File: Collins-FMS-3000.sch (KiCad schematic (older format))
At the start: 24 parts, among them J3 Conn_02x04_Odd_Even, U2 MCP23017_SO, U3 MCP23017_SO, U4 IS31FL3733B

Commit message: Use perfect 0402 pad dimensions
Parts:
- C1, C2, C22, C23, C24, C25, C26, C27, C28, C3, C4: footprint Capacitor_SMD:C_0402_1005Metric -> Collins-FMS-3000:Perfect_0402
- R6, R7: footprint Resistor_SMD:R_0402_1005Metric -> Collins-FMS-3000:Perfect_0402
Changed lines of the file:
@@
 F 0 "C2" H 3442 3196 50  0000 L CNN
 F 1 "100nf" H 3442 3105 50  0000 L CNN
-F 2 "Capacitor_SMD:C_0402_1005Metric" H 3350 3150 50  0001 C CNN
+F 2 "Collins-FMS-3000:Perfect_0402" H 3350 3150 50  0001 C CNN
 F 3 "~" H 3350 3150 50  0001 C CNN
 F 4 "0402" H 3350 3150 50  0001 C CNN "JLC"
@@
 F 0 "C1" H 3092 3196 50  0000 L CNN
 F 1 "1uF" H 3092 3105 50  0000 L CNN
-F 2 "Capacitor_SMD:C_0402_1005Metric" H 3000 3150 50  0001 C CNN
+F 2 "Collins-FMS-3000:Perfect_0402" H 3000 3150 50  0001 C CNN
 F 3 "~" H 3000 3150 50  0001 C CNN
 F 4 "0402" H 3000 3150 50  0001 C CNN "JLC"
@@
 F 0 "C4" H 4192 3196 50  0000 L CNN
 F 1 "100nf" H 4192 3105 50  0000 L CNN
-F 2 "Capacitor_SMD:C_0402_1005Metric" H 4100 3150 50  0001 C CNN
+F 2 "Collins-FMS-3000:Perfect_0402" H 4100 3150 50  0001 C CNN
 F 3 "~" H 4100 3150 50  0001 C CNN
 F 4 "0402" H 4100 3150 50  0001 C CNN "JLC"
@@
 F 0 "C3" H 3842 3196 50  0000 L CNN
 F 1 "1uF" H 3842 3105 50  0000 L CNN
-F 2 "Capacitor_SMD:C_0402_1005Metric" H 3750 3150 50  0001 C CNN
+F 2 "Collins-FMS-3000:Perfect_0402" H 3750 3150 50  0001 C CNN
 F 3 "~" H 3750 3150 50  0001 C CNN
 F 4 "0402" H 3750 3150 50  0001 C CNN "JLC"
@@
 F 0 "C22" H 6892 1246 50  0000 L CNN
 F 1 "470nf" H 6892 1155 50  0000 L CNN
-F 2 "Capacitor_SMD:C_0402_1005Metric" H 6800 1200 50  0001 C CNN
+F 2 "Collins-FMS-3000:Perfect_0402" H 6800 1200 50  0001 C CNN
 F 3 "~" H 6800 1200 50  0001 C CNN
 F 4 "0402" H 6800 1200 50  0001 C CNN "JLC"
@@
 F 0 "C25" H 7292 1246 50  0000 L CNN
 F 1 "100nf" H 7292 1155 50  0000 L CNN
-F 2 "Capacitor_SMD:C_0402_1005Metric" H 7200 1200 50  0001 C CNN
+F 2 "Collins-FMS-3000:Perfect_0402" H 7200 1200 50  0001 C CNN
 F 3 "~" H 7200 1200 50  0001 C CNN
 F 4 "0402" H 7200 1200 50  0001 C CNN "JLC"
@@
 F 0 "C23" H 6892 1546 50  0000 L CNN
 F 1 "470nf" H 6892 1455 50  0000 L CNN
-F 2 "Capacitor_SMD:C_0402_1005Metric" H 6800 1500 50  0001 C CNN
+F 2 "Collins-FMS-3000:Perfect_0402" H 6800 1500 50  0001 C CNN
 F 3 "~" H 6800 1500 50  0001 C CNN
 F 4 "0402" H 6800 1500 50  0001 C CNN "JLC"
@@
 F 0 "C26" H 7292 1546 50  0000 L CNN
 F 1 "100nf" H 7292 1455 50  0000 L CNN
-F 2 "Capacitor_SMD:C_0402_1005Metric" H 7200 1500 50  0001 C CNN
+F 2 "Collins-FMS-3000:Perfect_0402" H 7200 1500 50  0001 C CNN
 F 3 "~" H 7200 1500 50  0001 C CNN
 F 4 "0402" H 7200 1500 50  0001 C CNN "JLC"
@@
 F 0 "C24" H 6892 1896 50  0000 L CNN
 F 1 "470nf" H 6892 1805 50  0000 L CNN
-F 2 "Capacitor_SMD:C_0402_1005Metric" H 6800 1850 50  0001 C CNN
+F 2 "Collins-FMS-3000:Perfect_0402" H 6800 1850 50  0001 C CNN
 F 3 "~" H 6800 1850 50  0001 C CNN
 F 4 "0402" H 6800 1850 50  0001 C CNN "JLC"
@@
 F 0 "C27" H 7292 1896 50  0000 L CNN
 F 1 "100nf" H 7292 1805 50  0000 L CNN
-F 2 "Capacitor_SMD:C_0402_1005Metric" H 7200 1850 50  0001 C CNN
+F 2 "Collins-FMS-3000:Perfect_0402" H 7200 1850 50  0001 C CNN
 F 3 "~" H 7200 1850 50  0001 C CNN
 F 4 "0402" H 7200 1850 50  0001 C CNN "JLC"
@@
 F 0 "C28" H 7292 3196 50  0000 L CNN
 F 1 "470nf" H 7292 3105 50  0000 L CNN
-F 2 "Capacitor_SMD:C_0402_1005Metric" H 7200 3150 50  0001 C CNN
+F 2 "Collins-FMS-3000:Perfect_0402" H 7200 3150 50  0001 C CNN
 F 3 "~" H 7200 3150 50  0001 C CNN
 F 4 "0402" H 7200 3150 50  0001 C CNN "JLC"
@@
 F 0 "R7" H 6909 2896 50  0000 L CNN
 F 1 "100k" H 6909 2805 50  0000 L CNN
-F 2 "Resistor_SMD:R_0402_1005Metric" H 6850 2850 50  0001 C CNN
+F 2 "Collins-FMS-3000:Perfect_0402" H 6850 2850 50  0001 C CNN
 F 3 "~" H 6850 2850 50  0001 C CNN
 F 4 "0402" H 6850 2850 50  0001 C CNN "JLC"
@@
 F 0 "R6" H 6759 3746 50  0000 L CNN
 F 1 "47k" H 6759 3655 50  0000 L CNN
-F 2 "Resistor_SMD:R_0402_1005Metric" H 6700 3700 50  0001 C CNN
+F 2 "Collins-FMS-3000:Perfect_0402" H 6700 3700 50  0001 C CNN
 F 3 "~" H 6700 3700 50  0001 C CNN
 F 4 "0402" H 6700 3700 50  0001 C CNN "JLC"

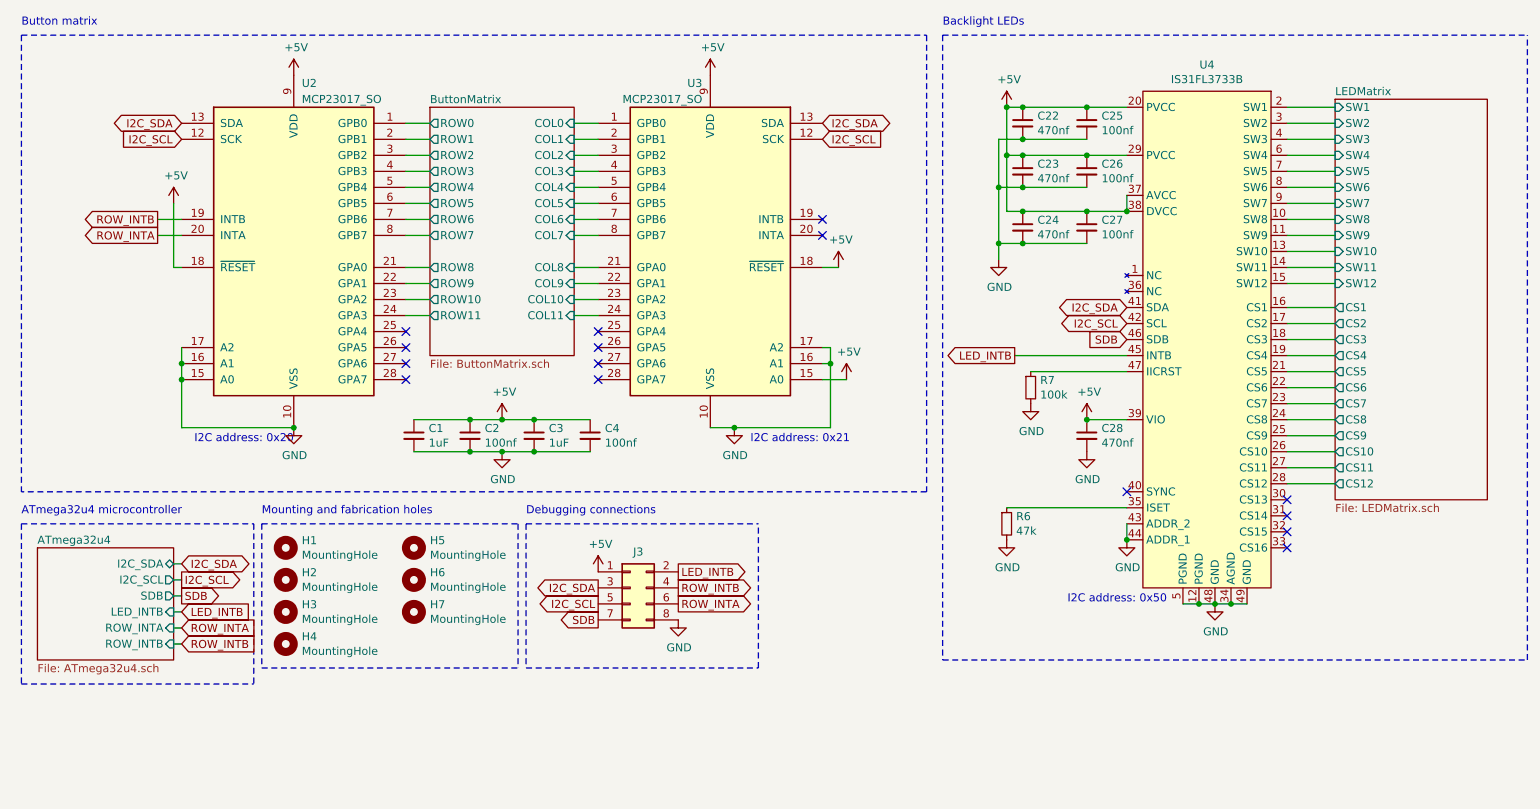
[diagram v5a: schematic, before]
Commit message: New PCB size and hole placement
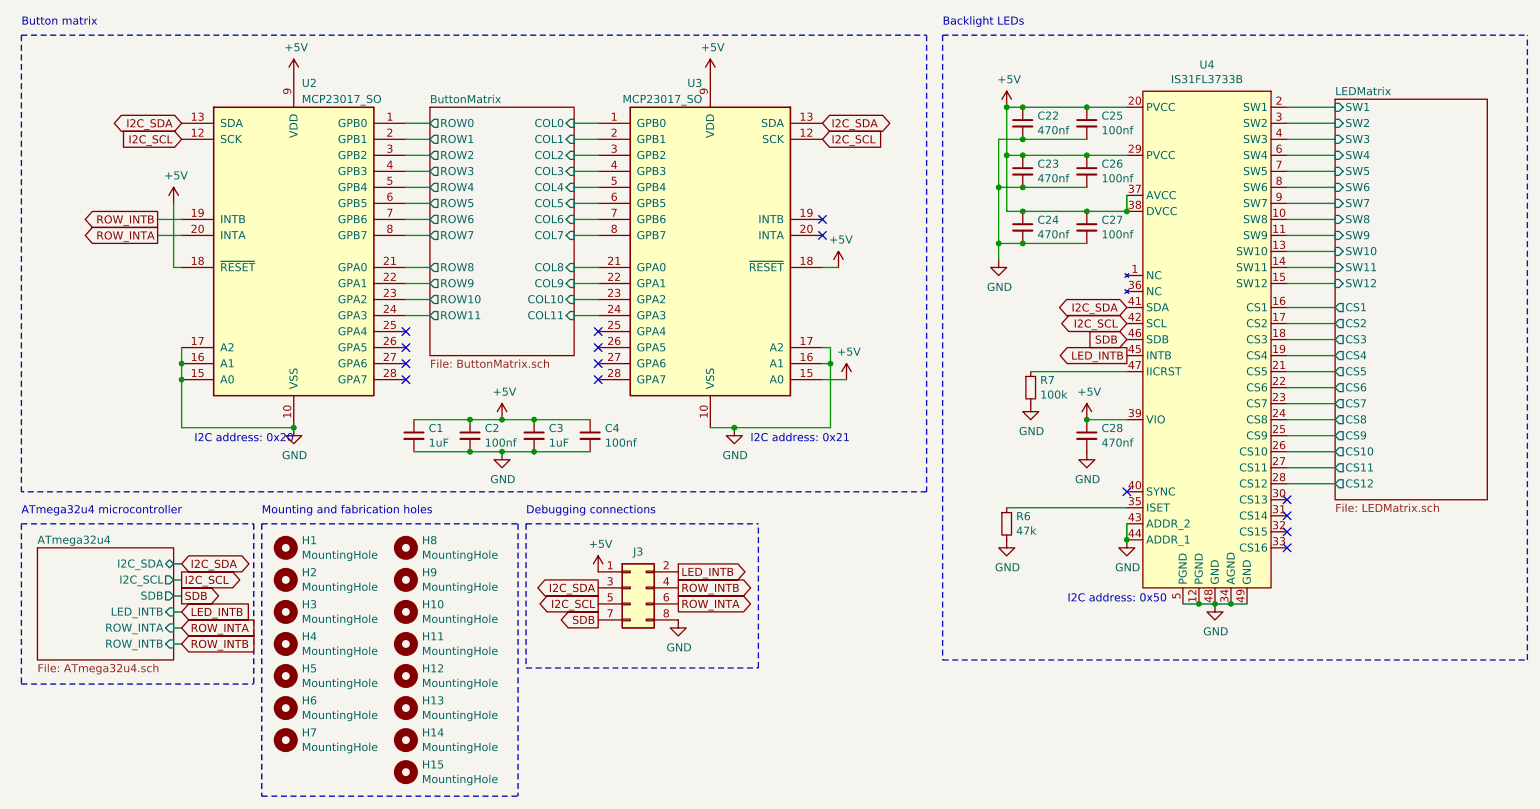
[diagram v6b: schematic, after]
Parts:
- added H10, H11, H12, H13, H14, H15, H8, H9: MountingHole, MountingHole:MountingHole_3.2mm_M3, symbol Mechanical:MountingHole
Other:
- moved on the sheet: H5, H6, H7
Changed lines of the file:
@@
 	1    0    0    -1
 $EndComp
-Wire Notes Line
-	2050 3700 2050 4600
 Text Notes 2050 3650 0    50   ~ 0
 Mounting and fabrication holes
@@
 L Mechanical:MountingHole H5
 U 1 1 618DF41E
-P 3000 3850
-F 0 "H5" H 3100 3896 50  0000 L CNN
-F 1 "MountingHole" H 3100 3805 50  0000 L CNN
-F 2 "Collins-FMS-3000:JLCPCB_Tooling_Hole" H 3000 3850 50  0001 C CNN
-F 3 "~" H 3000 3850 50  0001 C CNN
-	1    3000 3850
+P 2200 4650
+F 0 "H5" H 2300 4696 50  0000 L CNN
+F 1 "MountingHole" H 2300 4605 50  0000 L CNN
+F 2 "Collins-FMS-3000:JLCPCB_Tooling_Hole" H 2200 4650 50  0001 C CNN
+F 3 "~" H 2200 4650 50  0001 C CNN
+	1    2200 4650
 	1    0    0    -1
 $EndComp
@@
 L Mechanical:MountingHole H6
 U 1 1 618DF424
-P 3000 4050
-F 0 "H6" H 3100 4096 50  0000 L CNN
-F 1 "MountingHole" H 3100 4005 50  0000 L CNN
-F 2 "Collins-FMS-3000:JLCPCB_Tooling_Hole" H 3000 4050 50  0001 C CNN
-F 3 "~" H 3000 4050 50  0001 C CNN
-	1    3000 4050
+P 2200 4850
+F 0 "H6" H 2300 4896 50  0000 L CNN
+F 1 "MountingHole" H 2300 4805 50  0000 L CNN
+F 2 "Collins-FMS-3000:JLCPCB_Tooling_Hole" H 2200 4850 50  0001 C CNN
+F 3 "~" H 2200 4850 50  0001 C CNN
+	1    2200 4850
 	1    0    0    -1
 $EndComp
@@
 L Mechanical:MountingHole H7
 U 1 1 618DF42A
-P 3000 4250
-F 0 "H7" H 3100 4296 50  0000 L CNN
-F 1 "MountingHole" H 3100 4205 50  0000 L CNN
-F 2 "Collins-FMS-3000:JLCPCB_Tooling_Hole" H 3000 4250 50  0001 C CNN
-F 3 "~" H 3000 4250 50  0001 C CNN
-	1    3000 4250
-	1    0    0    -1
-$EndComp
-Wire Notes Line
-	3650 3700 3650 4600
-Wire Notes Line
-	2050 4600 3650 4600
+P 2200 5050
+F 0 "H7" H 2300 5096 50  0000 L CNN
+F 1 "MountingHole" H 2300 5005 50  0000 L CNN
+F 2 "Collins-FMS-3000:JLCPCB_Tooling_Hole" H 2200 5050 50  0001 C CNN
+F 3 "~" H 2200 5050 50  0001 C CNN
+	1    2200 5050
+	1    0    0    -1
+$EndComp
 Wire Notes Line
 	2050 3700 3650 3700
-Text GLabel 6750 2650 0    50   Output ~ 0
+Text GLabel 7450 2650 0    50   Output ~ 0
 LED_INTB
 Text GLabel 1550 4250 2    50   Input ~ 0
@@
 NoConn ~ 4150 2700
 NoConn ~ 4150 2800
-Wire Wire Line
-	6750 2650 7450 2650
 Wire Wire Line
 	1400 1900 1550 1900
@@
 	1    0    0    -1
 $EndComp
+$Comp
+L Mechanical:MountingHole H8
+U 1 1 61AD38B3
+P 2950 3850
+F 0 "H8" H 3050 3896 50  0000 L CNN
+F 1 "MountingHole" H 3050 3805 50  0000 L CNN
+F 2 "MountingHole:MountingHole_3.2mm_M3" H 2950 3850 50  0001 C CNN
+F 3 "~" H 2950 3850 50  0001 C CNN
+	1    2950 3850
+	1    0    0    -1
+$EndComp
+$Comp
+L Mechanical:MountingHole H10
+U 1 1 61AD8E9A
+P 2950 4250
+F 0 "H10" H 3050 4296 50  0000 L CNN
+F 1 "MountingHole" H 3050 4205 50  0000 L CNN
+F 2 "MountingHole:MountingHole_3.2mm_M3" H 2950 4250 50  0001 C CNN
+F 3 "~" H 2950 4250 50  0001 C CNN
+	1    2950 4250
+	1    0    0    -1
+$EndComp
+$Comp
+L Mechanical:MountingHole H12
+U 1 1 61ADE53B
+P 2950 4650
+F 0 "H12" H 3050 4696 50  0000 L CNN
+F 1 "MountingHole" H 3050 4605 50  0000 L CNN
+F 2 "MountingHole:MountingHole_3.2mm_M3" H 2950 4650 50  0001 C CNN
+F 3 "~" H 2950 4650 50  0001 C CNN
+	1    2950 4650
+	1    0    0    -1
+$EndComp
+$Comp
+L Mechanical:MountingHole H9
+U 1 1 61AE9DE8
+P 2950 4050
+F 0 "H9" H 3050 4096 50  0000 L CNN
+F 1 "MountingHole" H 3050 4005 50  0000 L CNN
+F 2 "MountingHole:MountingHole_3.2mm_M3" H 2950 4050 50  0001 C CNN
+F 3 "~" H 2950 4050 50  0001 C CNN
+	1    2950 4050
+	1    0    0    -1
+$EndComp
+$Comp
+L Mechanical:MountingHole H11
+U 1 1 61AE9DEE
+P 2950 4450
+F 0 "H11" H 3050 4496 50  0000 L CNN
+F 1 "MountingHole" H 3050 4405 50  0000 L CNN
+F 2 "MountingHole:MountingHole_3.2mm_M3" H 2950 4450 50  0001 C CNN
+F 3 "~" H 2950 4450 50  0001 C CNN
+	1    2950 4450
+	1    0    0    -1
+$EndComp
+$Comp
+L Mechanical:MountingHole H13
+U 1 1 61AE9DF4
+P 2950 4850
+F 0 "H13" H 3050 4896 50  0000 L CNN
+F 1 "MountingHole" H 3050 4805 50  0000 L CNN
+F 2 "MountingHole:MountingHole_3.2mm_M3" H 2950 4850 50  0001 C CNN
+F 3 "~" H 2950 4850 50  0001 C CNN
+	1    2950 4850
+	1    0    0    -1
+$EndComp
+$Comp
+L Mechanical:MountingHole H14
+U 1 1 61AEFD2F
+P 2950 5050
+F 0 "H14" H 3050 5096 50  0000 L CNN
+F 1 "MountingHole" H 3050 5005 50  0000 L CNN
+F 2 "MountingHole:MountingHole_3.2mm_M3" H 2950 5050 50  0001 C CNN
+F 3 "~" H 2950 5050 50  0001 C CNN
+	1    2950 5050
+	1    0    0    -1
+$EndComp
+$Comp
+L Mechanical:MountingHole H15
+U 1 1 61AEFD35
+P 2950 5250
+F 0 "H15" H 3050 5296 50  0000 L CNN
+F 1 "MountingHole" H 3050 5205 50  0000 L CNN
+F 2 "MountingHole:MountingHole_3.2mm_M3" H 2950 5250 50  0001 C CNN
+F 3 "~" H 2950 5250 50  0001 C CNN
+	1    2950 5250
+	1    0    0    -1
+$EndComp
+Wire Notes Line
+	2050 5400 3650 5400
+Wire Notes Line
+	2050 3700 2050 5400
+Wire Notes Line
+	3650 3700 3650 5400
 $EndSCHEMATC

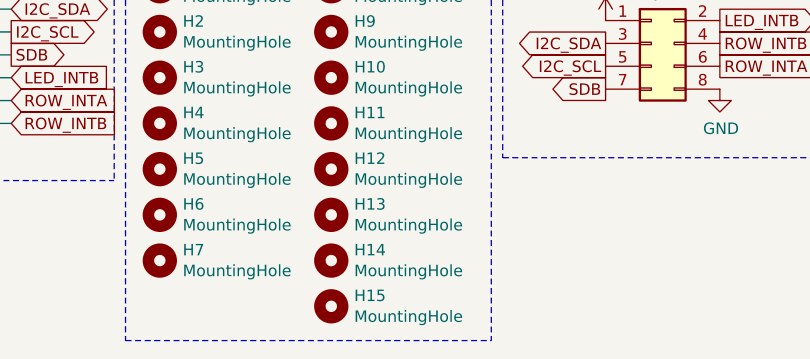
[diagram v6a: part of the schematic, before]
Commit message: All buttons moved to new layout
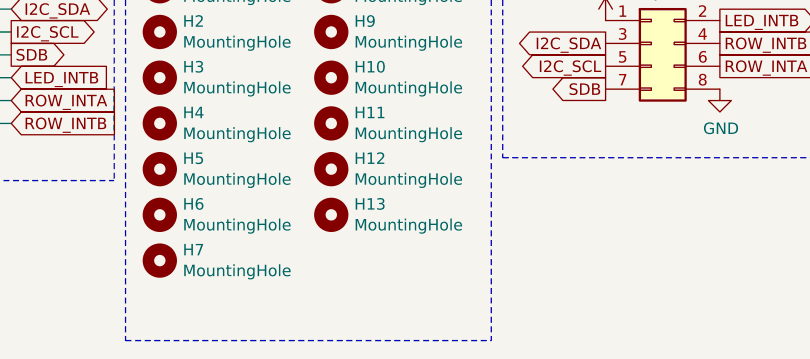
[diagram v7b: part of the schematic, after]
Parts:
- removed H14, H15: MountingHole, MountingHole:MountingHole_3.2mm_M3, symbol Mechanical:MountingHole
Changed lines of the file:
@@
-	1    0    0    -1
-$EndComp
-$Comp
-L Mechanical:MountingHole H14
-U 1 1 61AEFD2F
-P 2950 5050
-F 0 "H14" H 3050 5096 50  0000 L CNN
-F 1 "MountingHole" H 3050 5005 50  0000 L CNN
-F 2 "MountingHole:MountingHole_3.2mm_M3" H 2950 5050 50  0001 C CNN
-F 3 "~" H 2950 5050 50  0001 C CNN
-	1    2950 5050
-	1    0    0    -1
-$EndComp
-$Comp
-L Mechanical:MountingHole H15
-U 1 1 61AEFD35
-P 2950 5250
-F 0 "H15" H 3050 5296 50  0000 L CNN
-F 1 "MountingHole" H 3050 5205 50  0000 L CNN
-F 2 "MountingHole:MountingHole_3.2mm_M3" H 2950 5250 50  0001 C CNN
-F 3 "~" H 2950 5250 50  0001 C CNN
-	1    2950 5250
 	1    0    0    -1
 $EndComp
